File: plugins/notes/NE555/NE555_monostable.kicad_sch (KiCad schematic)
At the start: 4 parts, among them U1 NE555P

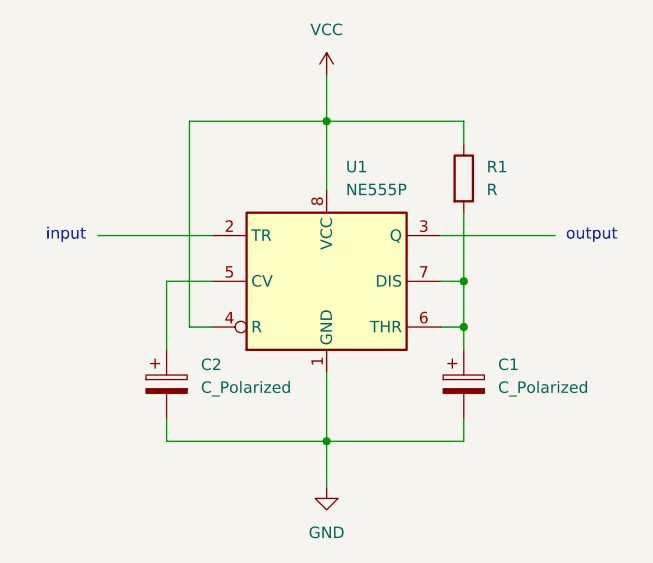
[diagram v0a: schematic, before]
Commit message: NE555: some signal drawings
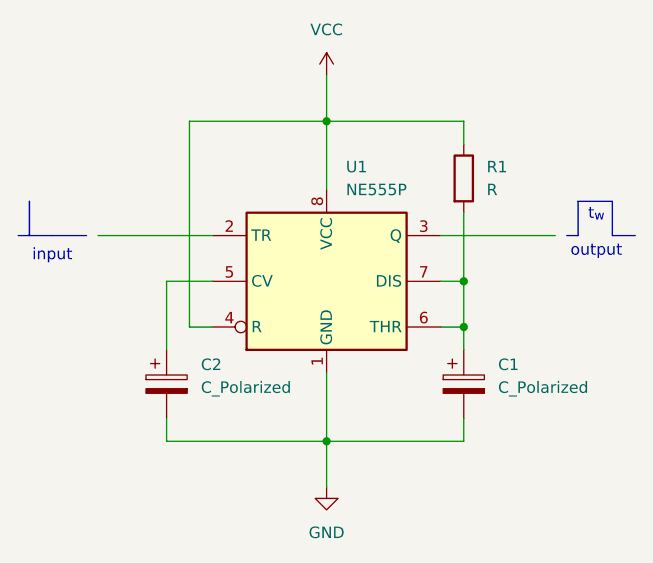
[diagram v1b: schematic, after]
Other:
- note added: "t_{w} output"
- note removed: "output"
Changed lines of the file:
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@@
 	(text "input"
 		(exclude_from_sim no)
-		(at 9.144 26.67 0)
+		(at 7.62 28.956 0)
 		(effects
 			(font
@@
 		)
 	)
-	(text "output"
+	(text "t_{w}\n\noutput"
 		(exclude_from_sim no)
-		(at 67.564 26.67 0)
+		(at 68.072 26.416 0)
 		(effects
 			(font
@@
 		)
 	)
+	(polyline
+		(pts
+			(xy 66.04 22.86) (xy 69.85 22.86)
+		)
+		(stroke
+			(width 0)
+			(type default)
+		)
+	)
+	(polyline
+		(pts
+			(xy 69.85 22.86) (xy 69.85 26.67)
+		)
+		(stroke
+			(width 0)
+			(type default)
+		)
+	)
 	(wire
 		(pts
@@
 		)
 	)
+	(polyline
+		(pts
+			(xy 66.04 26.67) (xy 66.04 22.86)
+		)
+		(stroke
+			(width 0)
+			(type default)
+		)
+	)
 	(wire
 		(pts
@@
 		)
 	)
+	(polyline
+		(pts
+			(xy 5.08 22.86) (xy 5.08 26.67)
+		)
+		(stroke
+			(width 0)
+			(type default)
+		)
+	)
+	(polyline
+		(pts
+			(xy 3.81 26.67) (xy 5.08 26.67)
+		)
+		(stroke
+			(width 0)
+			(type default)
+		)
+	)
+	(polyline
+		(pts
+			(xy 5.08 22.86) (xy 5.08 26.67)
+		)
+		(stroke
+			(width 0)
+			(type default)
+		)
+	)
+	(polyline
+		(pts
+			(xy 69.85 26.67) (xy 72.39 26.67)
+		)
+		(stroke
+			(width 0)
+			(type default)
+		)
+	)
 	(wire
 		(pts
@@
 		)
 	)
+	(polyline
+		(pts
+			(xy 64.77 26.67) (xy 66.04 26.67)
+		)
+		(stroke
+			(width 0)
+			(type default)
+		)
+	)
 	(wire
 		(pts
@@
 		)
 		(stroke
+			(width 0)
+			(type default)
+		)
+	)
+	(polyline
+		(pts
+			(xy 5.08 26.67) (xy 7.62 26.67)
+		)
+		(stroke
+			(width 0)
+			(type default)
+		)
+	)
+	(polyline
+		(pts
+			(xy 7.62 26.67) (xy 11.43 26.67)
+		)
+		(stroke
